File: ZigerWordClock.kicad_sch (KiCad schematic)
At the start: 16 parts, among them U1 BTF-5V-060L-B_SK9822_LED_Stri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, U10 BTF-5V-060L-B_SK9822_LED_Stri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, U11 BTF-5V-060L-B_SK9822_LED_Stri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, U12 BTF-5V-060L-B_SK9822_LED_Stri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, U13 BTF-5V-060L-B_SK9822_LED_Stri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, U14 BTF-5V-060L-B_SK9822_LED_Stri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, U15 BTF-5V-060L-B_SK9822_LED_Stri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, U16 BTF-5V-060L-B_SK9822_LED_Stri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, U2 BTF-5V-060L-B_SK9822_LED_Stri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, U3 BTF-5V-060L-B_SK9822_LED_Stri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, U4 BTF-5V-060L-B_SK9822_LED_Stri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, U5 BTF-5V-060L-B_SK9822_LED_Stri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, U6 BTF-5V-060L-B_SK9822_LED_Stri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, U7 BTF-5V-060L-B_SK9822_LED_Stri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, U8 BTF-5V-060L-B_SK9822_LED_Stri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, U9 BTF-5V-060L-B_SK9822_LED_Stri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

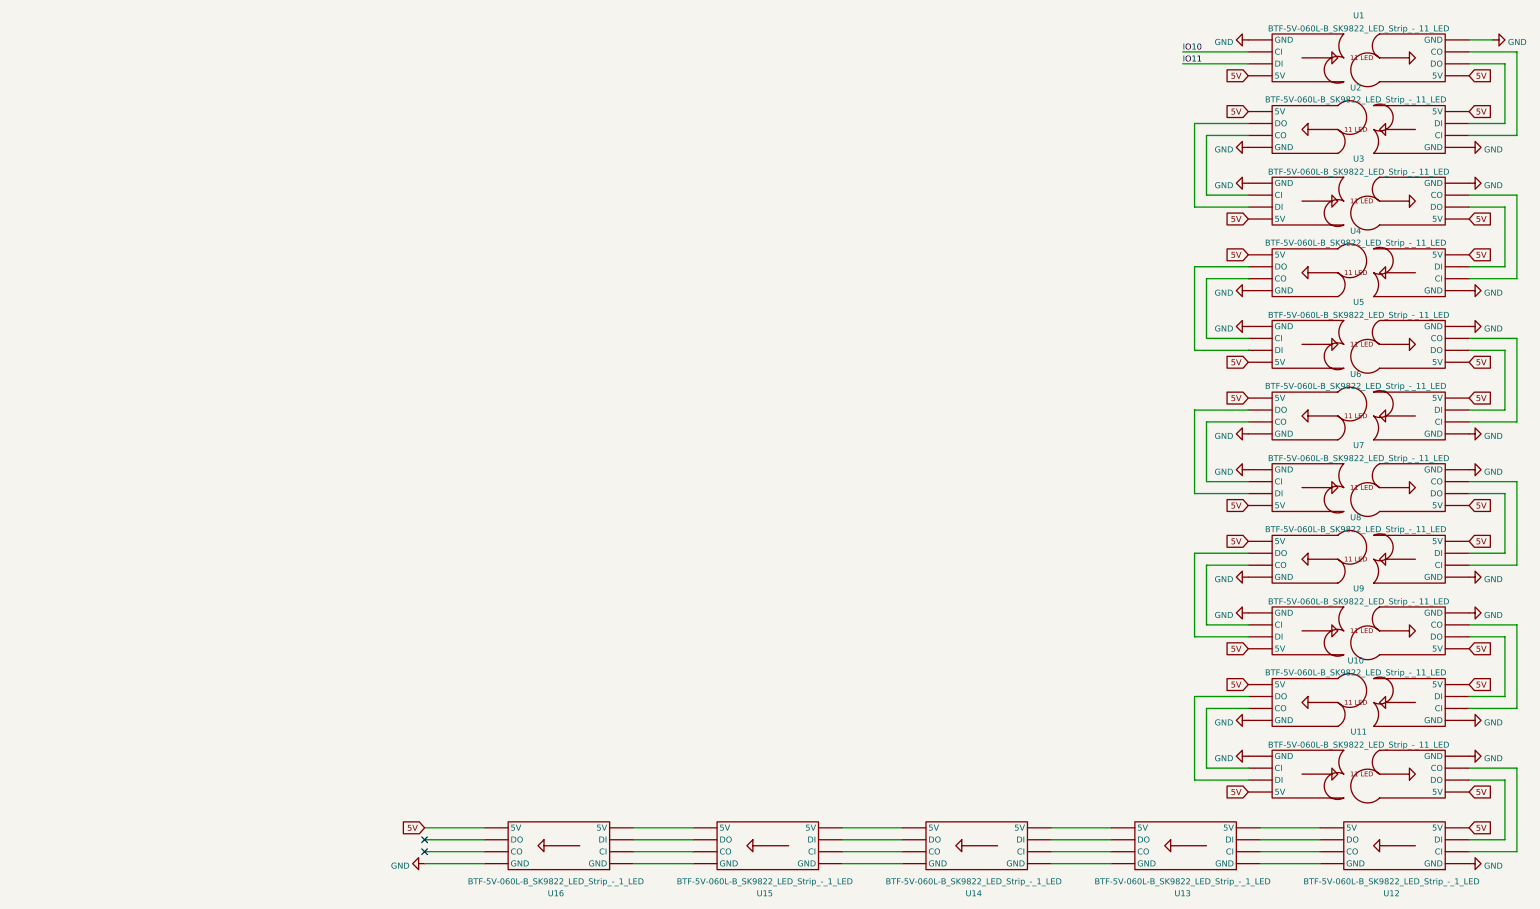
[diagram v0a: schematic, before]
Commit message: Added LevelShifter
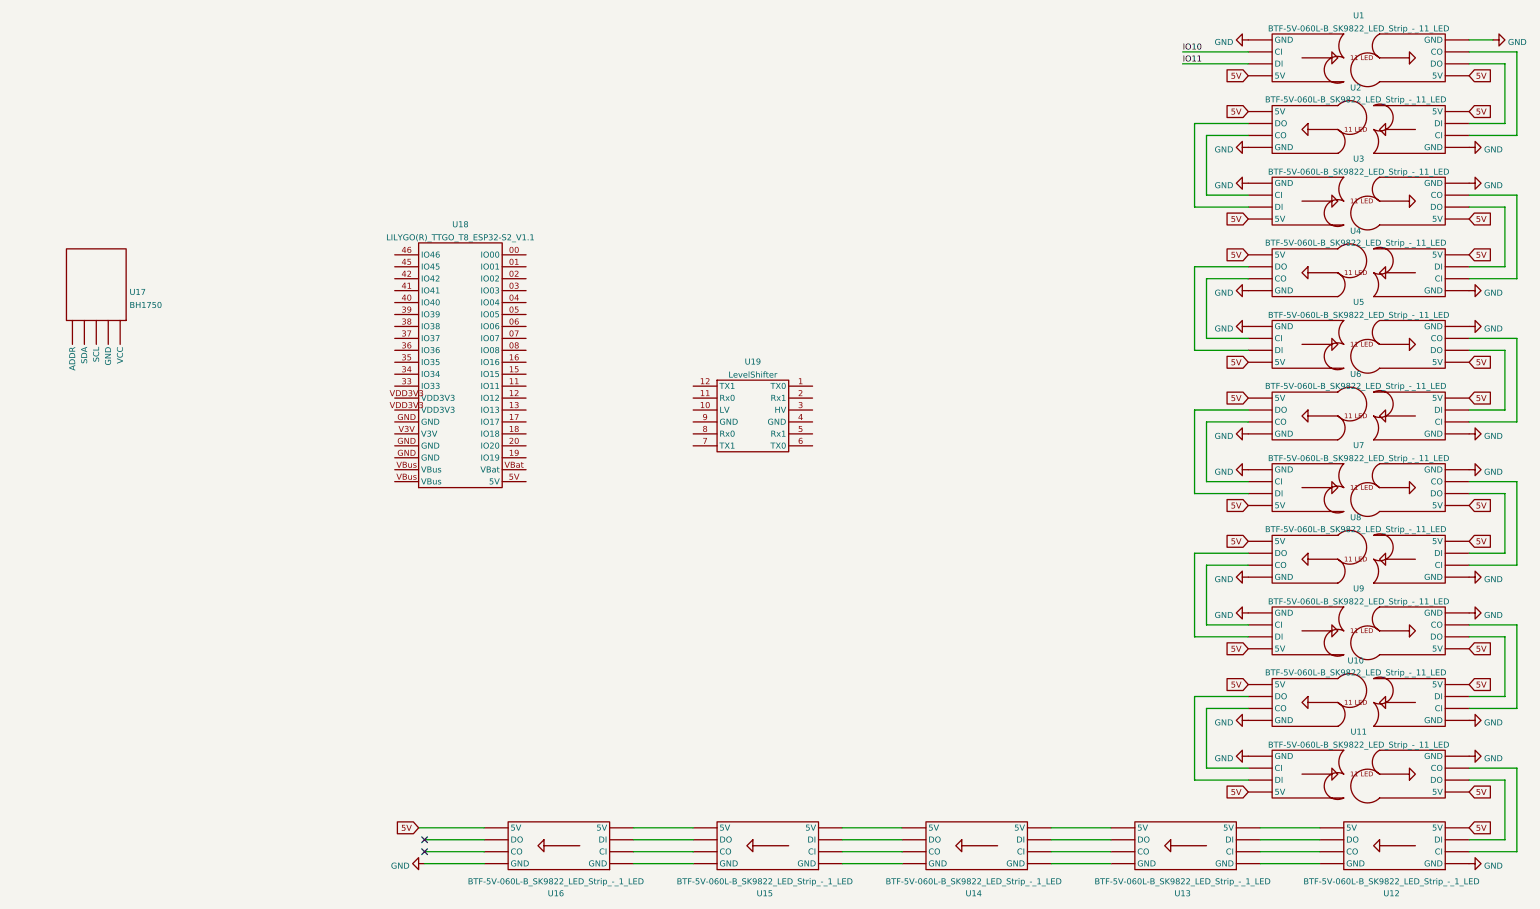
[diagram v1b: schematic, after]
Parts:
- added U17: BH1750, WordClock Footprint Library:BH1750 Breakout Board, symbol WordClock Symbol Library:BH1750
- added U18: LILYGO(R)_TTGO_T8_ESP32-S2_V1.1, WordClock Footprint Library:LILYGO® TTGO T8 ESP32-S2 V1.1, symbol WordClock Symbol Library:LILYGO(R)_TTGO_T8_ESP32-S2_V1.1
- added U19: LevelShifter, WordClock Footprint Library:LevelShifter, symbol WordClock Symbol Library:LevelShifter
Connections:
- net at U13. (GND): now also U14. (GND); no longer U12. (GND)
- net at U15. (GND): now also U16. (GND); no longer U14. (GND)
- new net: U6. (GND), U7. (GND) (x2)
- new net: U7. (GND), U8. (GND) (x2)
- new net: U11. (GND), U12. (GND) (x2)
- new net: U12. (GND), U13. (GND) (x4)
- new net: U10. (GND), U9. (GND) (x2)
- new net: U8. (GND), U9. (GND) (x2)
- new net: U14. (GND), U15. (GND) (x4)
- new net: U13. (GND), U14. (GND) (x3)
- new net: U5. (GND), U6. (GND) (x2)
- new net: U10. (GND), U11. (GND) (x2)
- new net: U2. (GND), U3. (GND) (x2)
- new net: U1. (GND), U2. (GND) (x2)
- new net: U3. (GND), U4. (GND) (x2)
- new net: U15. (GND), U16. (GND) (x3)
- new net: U4. (GND), U5. (GND) (x2)
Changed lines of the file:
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@@
+    (stroke (width 0) (type default) (color 0 0 0 0))
+  )
+  (wire (pts (xy 154.94 203.2) (xy 168.91 203.2))
     (stroke (width 0) (type default) (color 0 0 0 0))
   )
@@
   )
   (wire (pts (xy 317.5 38.1) (xy 331.47 38.1))
-    (stroke (width 0) (type default) (color 0 0 0 0))
-  )
-  (wire (pts (xy 156.21 203.2) (xy 168.91 203.2))
     (stroke (width 0) (type default) (color 0 0 0 0))
   )
@@
     )
   )
-  (global_label "5V" (shape input) (at 156.21 203.2 180) (fields_autoplaced)
+  (global_label "5V" (shape input) (at 154.94 203.2 180) (fields_autoplaced)
     (effects (font (size 1.27 1.27)) (justify right))
-    (property "Intersheet References" "${INTERSHEET_REFS}" (id 0) (at 151.4988 203.2794 0)
+    (property "Intersheet References" "${INTERSHEET_REFS}" (id 0) (at 150.2288 203.2794 0)
       (effects (font (size 1.27 1.27)) (justify right) hide)
     )
@@
     (pin "")
     (pin "")
+  )
+  (symbol (lib_id "WordClock Symbol Library:LevelShifter") (at 226.06 105.41 0) (unit 1)
+    (in_bom yes) (on_board yes) (fields_autoplaced)
+    (property "Reference" "U19" (id 0) (at 226.06 104.0343 0))
+    (property "Value" "LevelShifter" (id 1) (at 226.06 106.8094 0))
+    (property "Footprint" "WordClock Footprint Library:LevelShifter" (id 2) (at 226.06 105.41 0)
+      (effects (font (size 1.27 1.27)) hide)
+    )
+    (property "Datasheet" "" (id 3) (at 226.06 105.41 0)
+      (effects (font (size 1.27 1.27)) hide)
+    )
+    (pin "1")
+    (pin "10")
+    (pin "11")
+    (pin "12")
+    (pin "2")
+    (pin "3")
+    (pin "4")
+    (pin "5")
+    (pin "6")
+    (pin "7")
+    (pin "8")
+    (pin "9")
   )
   (symbol (lib_id "power:GND") (at 331.47 88.9 270) (unit 1)
@@
     (pin "")
   )
+  (symbol (lib_id "WordClock Symbol Library:LILYGO(R)_TTGO_T8_ESP32-S2_V1.1") (at 163.83 78.74 0) (unit 1)
+    (in_bom yes) (on_board yes) (fields_autoplaced)
+    (property "Reference" "U18" (id 0) (at 163.83 74.8243 0))
+    (property "Value" "LILYGO(R)_TTGO_T8_ESP32-S2_V1.1" (id 1) (at 163.83 77.5994 0))
+    (property "Footprint" "WordClock Footprint Library:LILYGO® TTGO T8 ESP32-S2 V1.1" (id 2) (at 163.83 78.74 0)
+      (effects (font (size 1.27 1.27)) hide)
+    )
+    (property "Datasheet" "" (id 3) (at 163.83 78.74 0)
+      (effects (font (size 1.27 1.27)) hide)
+    )
+    (pin "00")
+    (pin "01")
+    (pin "02")
+    (pin "03")
+    (pin "04")
+    (pin "05")
+    (pin "06")
+    (pin "07")
+    (pin "08")
+    (pin "11")
+    (pin "12")
+    (pin "13")
+    (pin "15")
+    (pin "16")
+    (pin "17")
+    (pin "18")
+    (pin "19")
+    (pin "20")
+    (pin "33")
+    (pin "34")
+    (pin "35")
+    (pin "36")
+    (pin "37")
+    (pin "38")
+    (pin "39")
+    (pin "40")
+    (pin "41")
+    (pin "42")
+    (pin "45")
+    (pin "46")
+    (pin "5V")
+    (pin "GND")
+    (pin "GND")
+    (pin "GND")
+    (pin "V3V")
+    (pin "VBat")
+    (pin "VBus")
+    (pin "VBus")
+    (pin "VDD3V3")
+    (pin "VDD3V3")
+  )
   (symbol (lib_id "power:GND") (at 331.47 96.52 270) (unit 1)
     (in_bom yes) (on_board yes) (fields_autoplaced)
@@
     (pin "1")
   )
+  (symbol (lib_id "WordClock Symbol Library:BH1750") (at 86.36 87.63 180) (unit 1)
+    (in_bom yes) (on_board yes) (fields_autoplaced)
+    (property "Reference" "U17" (id 0) (at 93.4212 89.2234 0)
+      (effects (font (size 1.27 1.27)) (justify right))
+    )
+    (property "Value" "BH1750" (id 1) (at 93.4212 91.9985 0)
+      (effects (font (size 1.27 1.27)) (justify right))
+    )
+    (property "Footprint" "WordClock Footprint Library:BH1750 Breakout Board" (id 2) (at 86.36 87.63 0)
+      (effects (font (size 1.27 1.27)) hide)
+    )
+    (property "Datasheet" "" (id 3) (at 86.36 87.63 0)
+      (effects (font (size 1.27 1.27)) hide)
+    )
+    (pin "")
+    (pin "")
+    (pin "")
+    (pin "")
+    (pin "")
+  )
   (sheet_instances
     (path "/" (page "1"))
@@
       (reference "U16") (unit 1) (value "BTF-5V-060L-B_SK9822_LED_Strip_-_1_LED") (footprint "WordClock Footprint Library:BTF-5V-060L-B SK9822 LED Strip - 1 Segment")
     )
-  )
+    (path "/f8df4375-570f-4eb0-868e-4f350bd24547"
+      (reference "U17") (unit 1) (value "BH1750") (footprint "WordClock Footprint Library:BH1750 Breakout Board")
+    )
+    (path "/6e30fc46-9f28-45c1-a45c-de224a55be3a"
+      (reference "U18") (unit 1) (value "LILYGO(R)_TTGO_T8_ESP32-S2_V1.1") (footprint "WordClock Footprint Library:LILYGO® TTGO T8 ESP32-S2 V1.1")
+    )
+    (path "/24ab50de-29df-47ec-a7d7-bb34d243d287"
+      (reference "U19") (unit 1) (value "LevelShifter") (footprint "WordClock Footprint Library:LevelShifter")
+    )
+  )

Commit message: Pins fixed in library
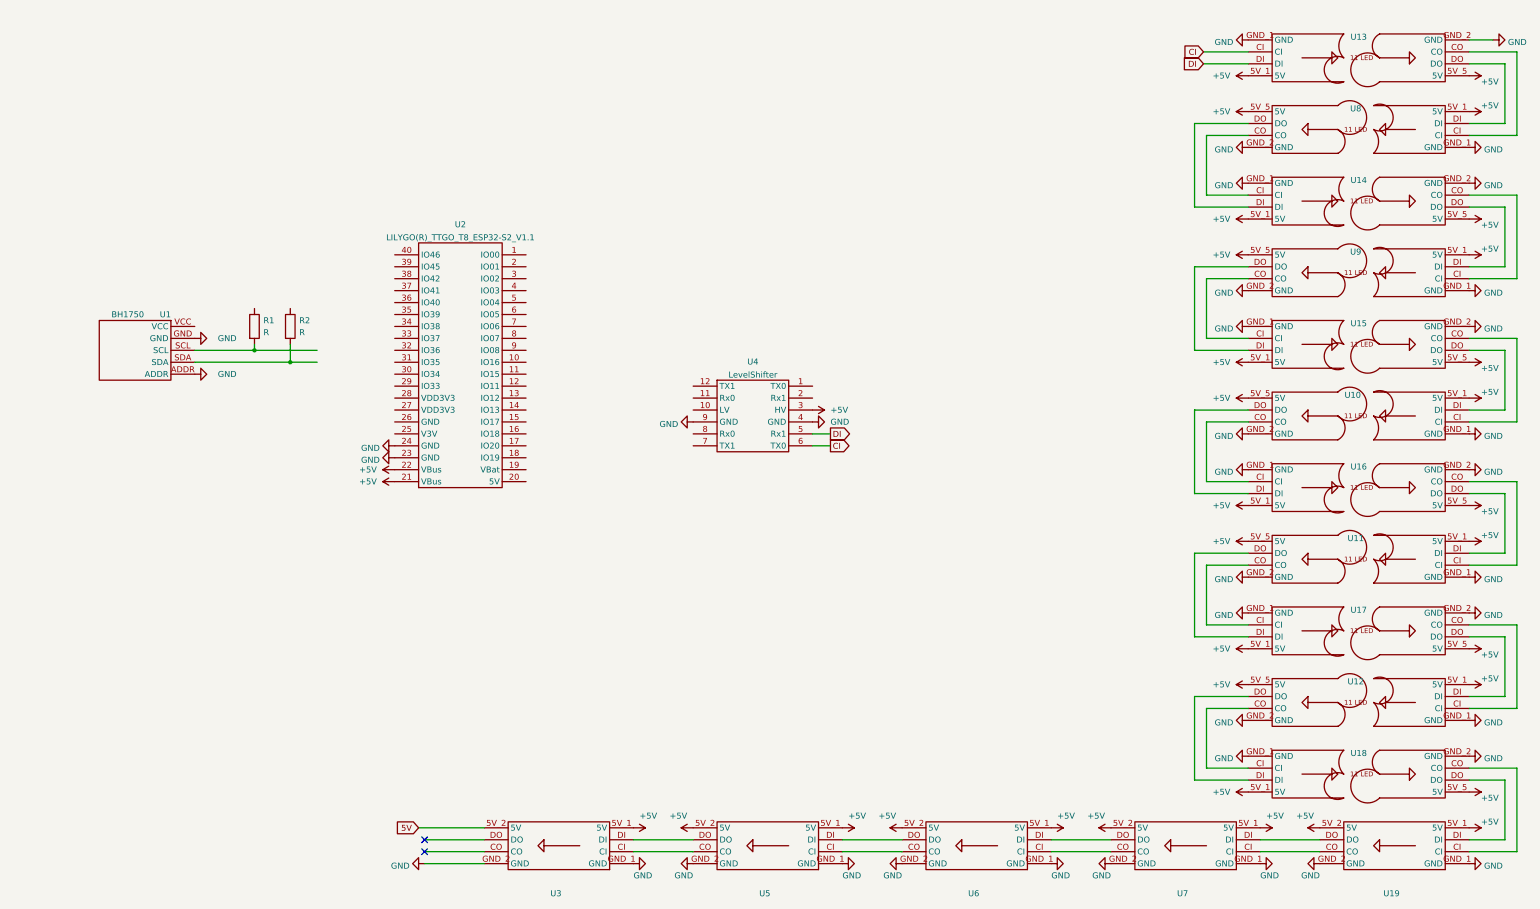
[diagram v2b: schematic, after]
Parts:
- added R1, R2: R, symbol Device:R
- U10: renamed from U6; footprint Footprint Library:BTF-5V-060L-B SK9822 LED Strip - 11 Segment -> WordClock Footprint Library:BTF-5V-060L-B SK9822 LED Strip - 11 Segment
- U11: renamed from U8; footprint Footprint Library:BTF-5V-060L-B SK9822 LED Strip - 11 Segment -> WordClock Footprint Library:BTF-5V-060L-B SK9822 LED Strip - 11 Segment
- U12: renamed from U10; footprint Footprint Library:BTF-5V-060L-B SK9822 LED Strip - 11 Segment -> WordClock Footprint Library:BTF-5V-060L-B SK9822 LED Strip - 11 Segment
- U13: renamed from U1; footprint Footprint Library:BTF-5V-060L-B SK9822 LED Strip - 11 Segment -> WordClock Footprint Library:BTF-5V-060L-B SK9822 LED Strip - 11 Segment
- U14: renamed from U3; footprint Footprint Library:BTF-5V-060L-B SK9822 LED Strip - 11 Segment -> WordClock Footprint Library:BTF-5V-060L-B SK9822 LED Strip - 11 Segment
- U15: renamed from U5; footprint Footprint Library:BTF-5V-060L-B SK9822 LED Strip - 11 Segment -> WordClock Footprint Library:BTF-5V-060L-B SK9822 LED Strip - 11 Segment
- U16: renamed from U7; footprint Footprint Library:BTF-5V-060L-B SK9822 LED Strip - 11 Segment -> WordClock Footprint Library:BTF-5V-060L-B SK9822 LED Strip - 11 Segment
- U17: renamed from U9; footprint Footprint Library:BTF-5V-060L-B SK9822 LED Strip - 11 Segment -> WordClock Footprint Library:BTF-5V-060L-B SK9822 LED Strip - 11 Segment
- U18: renamed from U11; footprint Footprint Library:BTF-5V-060L-B SK9822 LED Strip - 11 Segment -> WordClock Footprint Library:BTF-5V-060L-B SK9822 LED Strip - 11 Segment
- U8: renamed from U2; footprint Footprint Library:BTF-5V-060L-B SK9822 LED Strip - 11 Segment -> WordClock Footprint Library:BTF-5V-060L-B SK9822 LED Strip - 11 Segment
- U9: renamed from U4; footprint Footprint Library:BTF-5V-060L-B SK9822 LED Strip - 11 Segment -> WordClock Footprint Library:BTF-5V-060L-B SK9822 LED Strip - 11 Segment
- renumbered U17 to U1, U12 to U19, U18 to U2, U16 to U3, U19 to U4, U15 to U5, U14 to U6, U13 to U7
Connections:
- net 5V: now also U3.5V_2 (5V); no longer U10. (GND), U11. (GND), U12. (GND), U13. (GND), U14. (GND), U15. (GND), U16. (GND), U17. (GND), U18. (GND), U19. (GND), U3. (GND), U8. (GND), U9. (GND)
- net GND: now also U1.ADDR, U1.GND, U10.GND_1 (GND), U10.GND_2 (GND), U11.GND_1 (GND), U11.GND_2 (GND), U12.GND_1 (GND), U12.GND_2 (GND), U13.GND_1 (GND), U13.GND_2 (GND), U14.GND_1 (GND), U14.GND_2 (GND), U15.GND_1 (GND), U15.GND_2 (GND), U16.GND_1 (GND), U16.GND_2 (GND), U17.GND_1 (GND), U17.GND_2 (GND), U18.GND_1 (GND), U18.GND_2 (GND), U19.GND_1 (GND), U19.GND_2 (GND), U2.23 (GND), U2.24 (GND), U3.GND_1 (GND), U3.GND_2 (GND), U4.4 (GND), U4.9 (GND), U5.GND_1 (GND), U5.GND_2 (GND), U6.GND_1 (GND), U6.GND_2 (GND), U7.GND_1 (GND), U7.GND_2 (GND), U8.GND_1 (GND), U8.GND_2 (GND), U9.GND_1 (GND), U9.GND_2 (GND); no longer U10. (GND), U11. (GND), U12. (GND), U13. (GND), U14. (GND), U15. (GND), U16. (GND), U17. (GND), U18. (GND), U19. (GND), U3. (GND), U8. (GND), U9. (GND)
- net +5V: now reaches U4.3 (HV)
- net +5V: now also U10.5V_1 (5V), U10.5V_5 (5V), U11.5V_1 (5V), U11.5V_5 (5V), U12.5V_1 (5V), U12.5V_5 (5V), U13.5V_1 (5V), U13.5V_5 (5V), U14.5V_1 (5V), U14.5V_5 (5V), U15.5V_1 (5V), U15.5V_5 (5V), U16.5V_1 (5V), U16.5V_5 (5V), U17.5V_1 (5V), U17.5V_5 (5V), U18.5V_1 (5V), U18.5V_5 (5V), U19.5V_1 (5V), U19.5V_2 (5V), U2.21 (VBus), U2.22 (VBus), U3.5V_1 (5V), U5.5V_1 (5V), U5.5V_2 (5V), U6.5V_1 (5V), U6.5V_2 (5V), U7.5V_1 (5V), U7.5V_2 (5V), U8.5V_1 (5V), U8.5V_5 (5V), U9.5V_1 (5V), U9.5V_5 (5V)
- net DI: now reaches U4.5 (Rx1)
- net DI: now also U13.DI
- net CI: now reaches U4.6 (TX0)
- net CI: now also U13.CI
- removed net IO10: U13. (GND)
- removed net IO11: U13. (GND)
- new net: R1.2, U1.SCL
- new net: U10.CO, U16.CI
- new net: U11.CI, U16.CO
- new net: U10.DO, U16.DI
- new net: U11.DI, U16.DO
- new net: U18.CO, U19.CI
- new net: U19.CO, U7.CI
- new net: U18.DO, U19.DI
- new net: U19.DO, U7.DI
- new net: U11.CO, U17.CI
- new net: U12.CI, U17.CO
- new net: U11.DO, U17.DI
- new net: U12.DI, U17.DO
- new net: U6.CI, U7.CO
- new net: U5.CI, U6.CO
- new net: U6.DI, U7.DO
- new net: U5.DI, U6.DO
- new net: U10.CI, U15.CO
- new net: U10.DI, U15.DO
- new net: U12.CO, U18.CI
- new net: U12.DO, U18.DI
- new net: U13.CO, U8.CI
- new net: U14.CI, U8.CO
- new net: U13.DO, U8.DI
- new net: U14.DI, U8.DO
- new net: R2.2, U1.SDA
- new net: U14.CO, U9.CI
- new net: U14.DO, U9.DI
- new net: U3.CI, U5.CO
- new net: U3.DI, U5.DO
- new net: U15.CI, U9.CO
- new net: U15.DI, U9.DO
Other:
- moved on the sheet: U2
